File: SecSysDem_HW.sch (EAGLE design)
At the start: 44 parts, among them J1 22-05-7078-07, J2 22-27-2021-02, T1 MOSFET_NCHANNEL_ENHANCEMENT2N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, T2 MOSFET_NCHANNEL_ENHANCEMENT2N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, T3 MOSFET_NCHANNEL_ENHANCEMENT2N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, U1 XPLAINED_MINI_PINOUT, U2 PCF8574_IO_EXPANDER, U3 MCP4706_DAC, U4 FT24C512A, X1 C-GRID-06-70553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

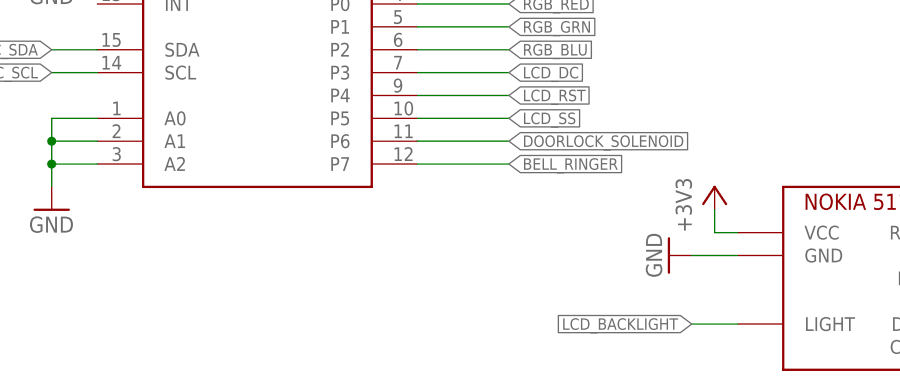
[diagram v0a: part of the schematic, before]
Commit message: Added NPN transistor to power the LCD backlight
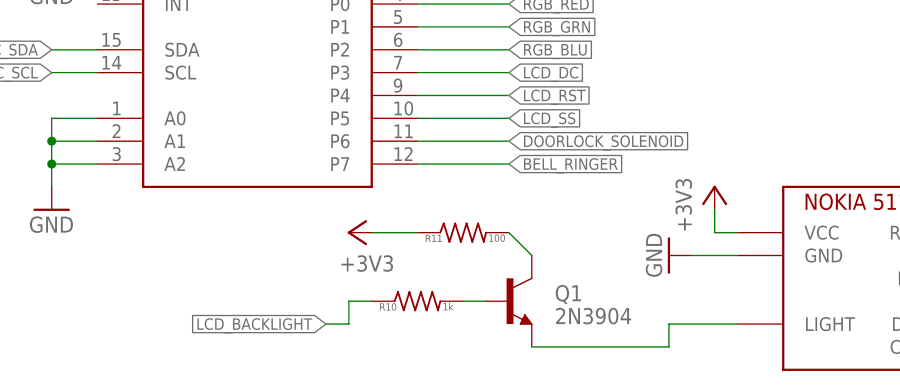
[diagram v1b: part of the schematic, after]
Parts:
- added Q1: 2N3904, SparkFun-DiscreteSemi:TRANSISTOR_NPNBC547
- added R10: 1k, Luke:RESISTOR0805
- added R11: 100, Luke:RESISTOR0805
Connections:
- new net N$18: Q1.C, R11.2
- new net N$7: Q1.B, R10.2
- net +3V3: now also R11.1
- net LCD_BACKLIGHT: now also Q1.E, R10.1
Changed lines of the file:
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@@
 <part name="V9" library="Luke" deviceset="VIA1" device="" value="3v3"/>
 <part name="+3V11" library="supply1" deviceset="+3V3" device=""/>
+<part name="Q1" library="SparkFun-DiscreteSemi" deviceset="TRANSISTOR_NPN" device="BC547" value="2N3904"/>
+<part name="+3V12" library="supply1" deviceset="+3V3" device=""/>
+<part name="R10" library="Luke" deviceset="RESISTOR" device="0805" value="1k"/>
+<part name="R11" library="Luke" deviceset="RESISTOR" device="0805" value="100"/>
 </parts>
 <sheets>
@@
 <instance part="V9" gate="G$1" x="86.36" y="99.06" rot="R180"/>
 <instance part="+3V11" gate="G$1" x="218.44" y="162.56"/>
+<instance part="Q1" gate="G$1" x="71.12" y="15.24"/>
+<instance part="+3V12" gate="G$1" x="53.34" y="22.86" rot="R90"/>
+<instance part="R10" gate="G$1" x="60.96" y="15.24"/>
+<instance part="R11" gate="G$1" x="66.04" y="22.86"/>
 </instances>
 <busses>
@@
 <pinref part="+3V11" gate="G$1" pin="+3V3"/>
 </segment>
+<segment>
+<pinref part="R11" gate="G$1" pin="1"/>
+<pinref part="+3V12" gate="G$1" pin="+3V3"/>
+<wire x1="60.96" y1="22.86" x2="55.88" y2="22.86" width="0.1524" layer="91"/>
+</segment>
 </net>
 <net name="PHOTORESISTOR" class="0">
@@
 <segment>
 <pinref part="U$3" gate="G$1" pin="LIGHT"/>
-<wire x1="96.52" y1="12.7" x2="91.44" y2="12.7" width="0.1524" layer="91"/>
-<label x="91.44" y="12.7" size="1.27" layer="95" rot="R180" xref="yes"/>
+<pinref part="Q1" gate="G$1" pin="E"/>
+<wire x1="96.52" y1="12.7" x2="88.9" y2="12.7" width="0.1524" layer="91"/>
+<wire x1="88.9" y1="12.7" x2="88.9" y2="10.16" width="0.1524" layer="91"/>
+<wire x1="88.9" y1="10.16" x2="73.66" y2="10.16" width="0.1524" layer="91"/>
+</segment>
+<segment>
+<wire x1="53.34" y1="15.24" x2="53.34" y2="12.7" width="0.1524" layer="91"/>
+<wire x1="53.34" y1="12.7" x2="50.8" y2="12.7" width="0.1524" layer="91"/>
+<label x="50.8" y="12.7" size="1.27" layer="95" rot="R180" xref="yes"/>
+<pinref part="R10" gate="G$1" pin="1"/>
+<wire x1="55.88" y1="15.24" x2="53.34" y2="15.24" width="0.1524" layer="91"/>
 </segment>
 </net>
@@
 </segment>
 </net>
+<net name="N$7" class="0">
+<segment>
+<pinref part="R10" gate="G$1" pin="2"/>
+<pinref part="Q1" gate="G$1" pin="B"/>
+<wire x1="66.04" y1="15.24" x2="68.58" y2="15.24" width="0.1524" layer="91"/>
+</segment>
+</net>
+<net name="N$18" class="0">
+<segment>
+<pinref part="Q1" gate="G$1" pin="C"/>
+<pinref part="R11" gate="G$1" pin="2"/>
+<wire x1="73.66" y1="20.32" x2="71.12" y2="22.86" width="0.1524" layer="91"/>
+</segment>
+</net>

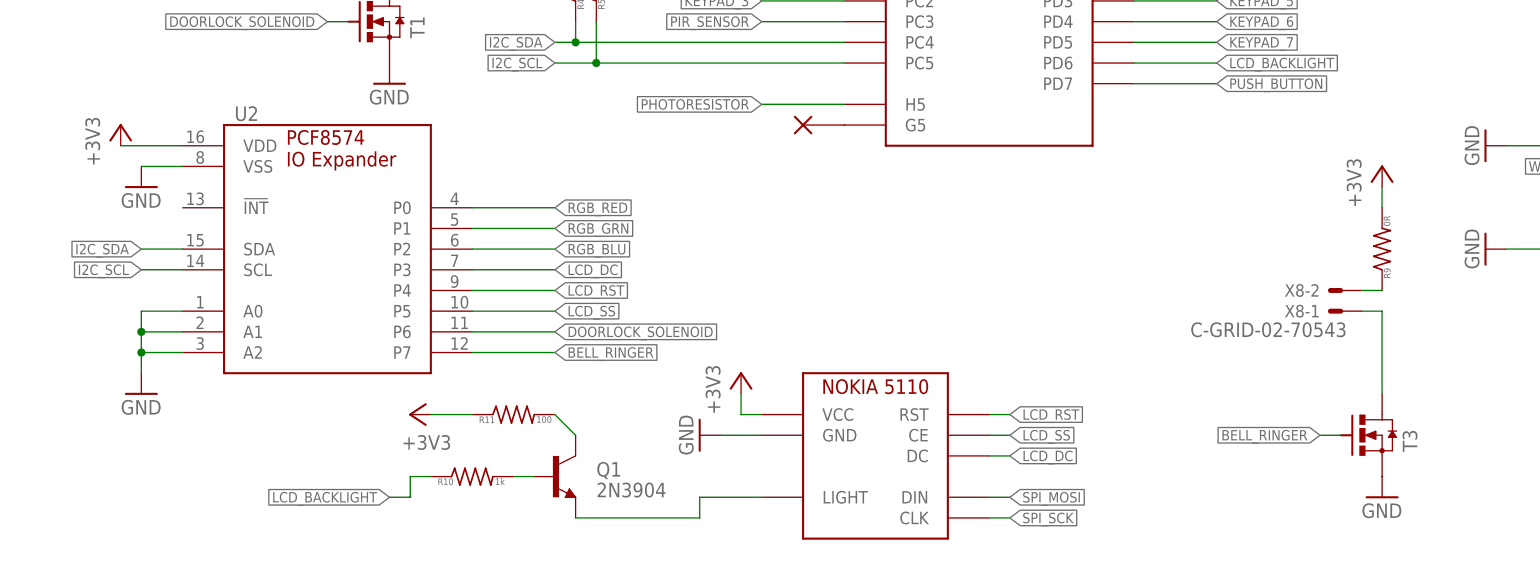
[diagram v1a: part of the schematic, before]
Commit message: Changed EEPROM address pins (A2, A1, A0) to VCC because of addressing conflicts with the RTC module on board EEPROM.
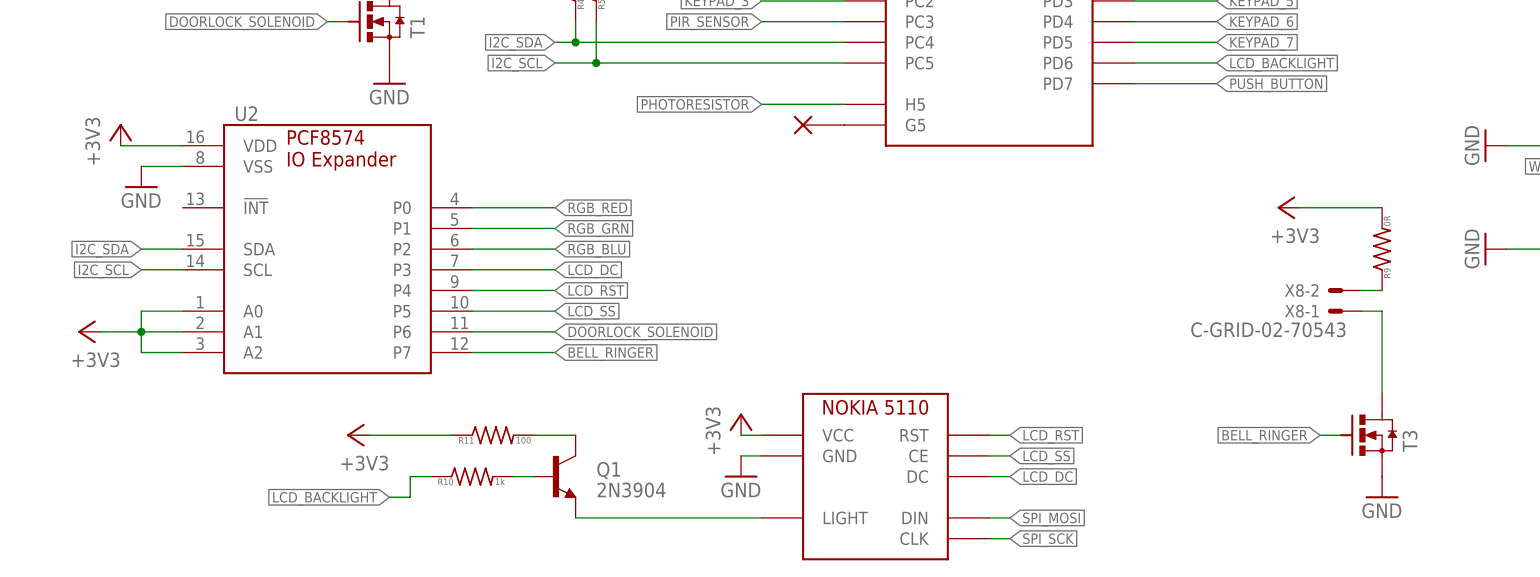
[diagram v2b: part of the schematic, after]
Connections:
- net +3V3: now also U2.A0, U2.A1, U2.A2
- net GND: no longer U2.A0, U2.A1, U2.A2
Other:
- moved on the sheet: R11
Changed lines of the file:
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@@
 <?xml version="1.0" encoding="utf-8"?>
 <!DOCTYPE eagle SYSTEM "eagle.dtd">
-<eagle version="6.5.0">
+<eagle version="7.3.0">
 <drawing>
 <settings>
@@
 <part name="+3V1" library="supply1" deviceset="+3V3" device=""/>
 <part name="U2" library="Luke" deviceset="PCF8574_IO_EXPANDER" device=""/>
-<part name="GND3" library="supply1" deviceset="GND" device=""/>
 <part name="GND4" library="supply1" deviceset="GND" device=""/>
 <part name="+3V2" library="supply1" deviceset="+3V3" device=""/>
@@
 <part name="R10" library="Luke" deviceset="RESISTOR" device="0805" value="1k"/>
 <part name="R11" library="Luke" deviceset="RESISTOR" device="0805" value="100"/>
+<part name="+3V13" library="supply1" deviceset="+3V3" device=""/>
 </parts>
 <sheets>
@@
 <instance part="+3V1" gate="G$1" x="91.44" y="106.68"/>
 <instance part="U2" gate="G$1" x="30.48" y="27.94"/>
-<instance part="GND3" gate="1" x="20.32" y="25.4"/>
 <instance part="GND4" gate="1" x="20.32" y="50.8"/>
 <instance part="+3V2" gate="G$1" x="17.78" y="58.42"/>
@@
 <instance part="GND10" gate="1" x="185.42" y="55.88" rot="R270"/>
 <instance part="GND11" gate="1" x="185.42" y="43.18" rot="R270"/>
-<instance part="U$3" gate="G$1" x="101.6" y="7.62"/>
-<instance part="GND12" gate="1" x="88.9" y="20.32" rot="R270"/>
-<instance part="+3V4" gate="G$1" x="93.98" y="27.94"/>
+<instance part="U$3" gate="G$1" x="101.6" y="5.08"/>
+<instance part="GND12" gate="1" x="93.98" y="15.24"/>
+<instance part="+3V4" gate="G$1" x="93.98" y="22.86"/>
 <instance part="X4" gate="-1" x="226.06" y="127"/>
 <instance part="X4" gate="-2" x="226.06" y="124.46"/>
@@
 <instance part="X8" gate="-1" x="167.64" y="35.56" rot="R180"/>
 <instance part="R9" gate="G$1" x="172.72" y="43.18" rot="R90"/>
-<instance part="+3V10" gate="G$1" x="172.72" y="53.34"/>
+<instance part="+3V10" gate="G$1" x="160.02" y="48.26" rot="R90"/>
 <instance part="V2" gate="G$1" x="147.32" y="93.98"/>
 <instance part="V3" gate="G$1" x="147.32" y="81.28"/>
@@
 <instance part="+3V11" gate="G$1" x="218.44" y="162.56"/>
 <instance part="Q1" gate="G$1" x="71.12" y="15.24"/>
-<instance part="+3V12" gate="G$1" x="53.34" y="22.86" rot="R90"/>
+<instance part="+3V12" gate="G$1" x="45.72" y="20.32" rot="R90"/>
 <instance part="R10" gate="G$1" x="60.96" y="15.24"/>
-<instance part="R11" gate="G$1" x="66.04" y="22.86"/>
+<instance part="R11" gate="G$1" x="63.5" y="20.32"/>
+<instance part="+3V13" gate="G$1" x="12.7" y="33.02" rot="R90"/>
 </instances>
 <busses>
@@
 </segment>
 <segment>
-<pinref part="U2" gate="G$1" pin="A0"/>
-<wire x1="25.4" y1="35.56" x2="20.32" y2="35.56" width="0.1524" layer="91"/>
-<pinref part="U2" gate="G$1" pin="A1"/>
-<wire x1="25.4" y1="33.02" x2="20.32" y2="33.02" width="0.1524" layer="91"/>
-<wire x1="20.32" y1="35.56" x2="20.32" y2="33.02" width="0.1524" layer="91"/>
-<pinref part="U2" gate="G$1" pin="A2"/>
-<wire x1="25.4" y1="30.48" x2="20.32" y2="30.48" width="0.1524" layer="91"/>
-<wire x1="20.32" y1="33.02" x2="20.32" y2="30.48" width="0.1524" layer="91"/>
-<junction x="20.32" y="33.02"/>
-<wire x1="20.32" y1="30.48" x2="20.32" y2="27.94" width="0.1524" layer="91"/>
-<junction x="20.32" y="30.48"/>
-<pinref part="GND3" gate="1" pin="GND"/>
-</segment>
-<segment>
 <pinref part="U2" gate="G$1" pin="VSS"/>
 <wire x1="25.4" y1="53.34" x2="20.32" y2="53.34" width="0.1524" layer="91"/>
@@
 <segment>
 <pinref part="U$3" gate="G$1" pin="GND"/>
-<wire x1="96.52" y1="20.32" x2="91.44" y2="20.32" width="0.1524" layer="91"/>
+<wire x1="96.52" y1="17.78" x2="93.98" y2="17.78" width="0.1524" layer="91"/>
 <pinref part="GND12" gate="1" pin="GND"/>
 </segment>
@@
 <segment>
 <pinref part="U$3" gate="G$1" pin="CLK"/>
-<wire x1="124.46" y1="10.16" x2="127" y2="10.16" width="0.1524" layer="91"/>
-<label x="127" y="10.16" size="1.27" layer="95" xref="yes"/>
+<wire x1="124.46" y1="7.62" x2="127" y2="7.62" width="0.1524" layer="91"/>
+<label x="127" y="7.62" size="1.27" layer="95" xref="yes"/>
 </segment>
 </net>
@@
 <segment>
 <pinref part="U$3" gate="G$1" pin="DIN"/>
-<wire x1="124.46" y1="12.7" x2="127" y2="12.7" width="0.1524" layer="91"/>
-<label x="127" y="12.7" size="1.27" layer="95" xref="yes"/>
+<wire x1="124.46" y1="10.16" x2="127" y2="10.16" width="0.1524" layer="91"/>
+<label x="127" y="10.16" size="1.27" layer="95" xref="yes"/>
 </segment>
 </net>
@@
 <segment>
 <pinref part="U$3" gate="G$1" pin="VCC"/>
-<wire x1="96.52" y1="22.86" x2="93.98" y2="22.86" width="0.1524" layer="91"/>
-<wire x1="93.98" y1="22.86" x2="93.98" y2="25.4" width="0.1524" layer="91"/>
+<wire x1="96.52" y1="20.32" x2="93.98" y2="20.32" width="0.1524" layer="91"/>
 <pinref part="+3V4" gate="G$1" pin="+3V3"/>
 </segment>
@@
 <pinref part="R9" gate="G$1" pin="2"/>
 <pinref part="+3V10" gate="G$1" pin="+3V3"/>
-<wire x1="172.72" y1="50.8" x2="172.72" y2="48.26" width="0.1524" layer="91"/>
+<wire x1="162.56" y1="48.26" x2="172.72" y2="48.26" width="0.1524" layer="91"/>
 </segment>
 <segment>
@@
 <pinref part="R11" gate="G$1" pin="1"/>
 <pinref part="+3V12" gate="G$1" pin="+3V3"/>
-<wire x1="60.96" y1="22.86" x2="55.88" y2="22.86" width="0.1524" layer="91"/>
+<wire x1="58.42" y1="20.32" x2="48.26" y2="20.32" width="0.1524" layer="91"/>
+</segment>
+<segment>
+<pinref part="U2" gate="G$1" pin="A0"/>
+<wire x1="25.4" y1="35.56" x2="20.32" y2="35.56" width="0.1524" layer="91"/>
+<pinref part="U2" gate="G$1" pin="A1"/>
+<wire x1="25.4" y1="33.02" x2="20.32" y2="33.02" width="0.1524" layer="91"/>
+<wire x1="20.32" y1="35.56" x2="20.32" y2="33.02" width="0.1524" layer="91"/>
+<pinref part="U2" gate="G$1" pin="A2"/>
+<wire x1="25.4" y1="30.48" x2="20.32" y2="30.48" width="0.1524" layer="91"/>
+<wire x1="20.32" y1="33.02" x2="20.32" y2="30.48" width="0.1524" layer="91"/>
+<junction x="20.32" y="33.02"/>
+<pinref part="+3V13" gate="G$1" pin="+3V3"/>
+<wire x1="15.24" y1="33.02" x2="20.32" y2="33.02" width="0.1524" layer="91"/>
 </segment>
 </net>
@@
 <pinref part="U$3" gate="G$1" pin="LIGHT"/>
 <pinref part="Q1" gate="G$1" pin="E"/>
-<wire x1="96.52" y1="12.7" x2="88.9" y2="12.7" width="0.1524" layer="91"/>
-<wire x1="88.9" y1="12.7" x2="88.9" y2="10.16" width="0.1524" layer="91"/>
-<wire x1="88.9" y1="10.16" x2="73.66" y2="10.16" width="0.1524" layer="91"/>
+<wire x1="96.52" y1="10.16" x2="73.66" y2="10.16" width="0.1524" layer="91"/>
 </segment>
 <segment>
@@
 <segment>
 <pinref part="U$3" gate="G$1" pin="DC"/>
-<wire x1="124.46" y1="17.78" x2="127" y2="17.78" width="0.1524" layer="91"/>
-<label x="127" y="17.78" size="1.27" layer="95" xref="yes"/>
+<wire x1="124.46" y1="15.24" x2="127" y2="15.24" width="0.1524" layer="91"/>
+<label x="127" y="15.24" size="1.27" layer="95" xref="yes"/>
 </segment>
 </net>
@@
 <segment>
 <pinref part="U$3" gate="G$1" pin="RST"/>
-<wire x1="124.46" y1="22.86" x2="127" y2="22.86" width="0.1524" layer="91"/>
-<label x="127" y="22.86" size="1.27" layer="95" xref="yes"/>
+<wire x1="124.46" y1="20.32" x2="127" y2="20.32" width="0.1524" layer="91"/>
+<label x="127" y="20.32" size="1.27" layer="95" xref="yes"/>
 </segment>
 </net>
@@
 <segment>
 <pinref part="U$3" gate="G$1" pin="CE"/>
-<wire x1="124.46" y1="20.32" x2="127" y2="20.32" width="0.1524" layer="91"/>
-<label x="127" y="20.32" size="1.27" layer="95" xref="yes"/>
+<wire x1="124.46" y1="17.78" x2="127" y2="17.78" width="0.1524" layer="91"/>
+<label x="127" y="17.78" size="1.27" layer="95" xref="yes"/>
 </segment>
 </net>
@@
 <pinref part="Q1" gate="G$1" pin="C"/>
 <pinref part="R11" gate="G$1" pin="2"/>
-<wire x1="73.66" y1="20.32" x2="71.12" y2="22.86" width="0.1524" layer="91"/>
-</segment>
-</net>
+<wire x1="73.66" y1="20.32" x2="68.58" y2="20.32" width="0.1524" layer="91"/>
+</segment>
+</net>
